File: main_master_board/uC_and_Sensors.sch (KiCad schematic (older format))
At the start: 39 parts, among them U1 NRF24L01+, U15 DSPIC33EP512GP806-I/PT, U16 DWM1000, U29 RGB_LED, U30 RGB_LED, U31 Si1900DL, U32 Si1900DL, U9 Si1900DL

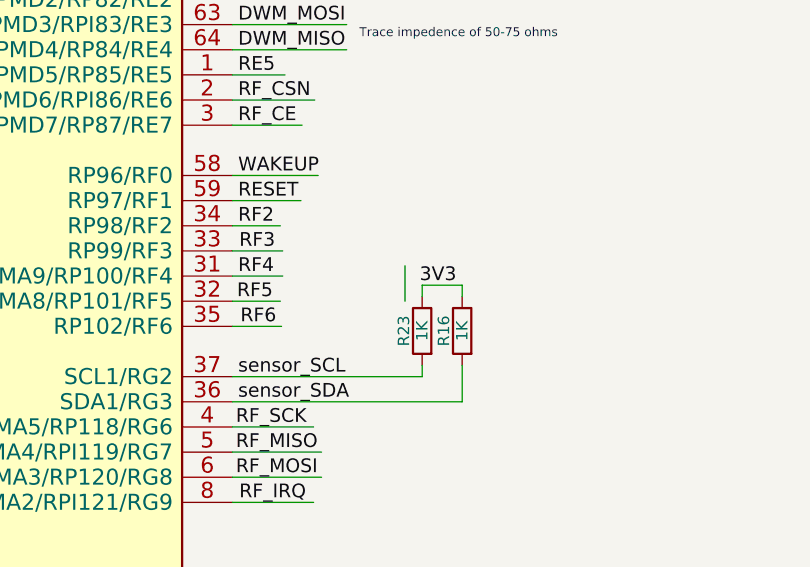
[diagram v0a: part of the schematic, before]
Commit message: Routed the 24-5 buck and added the dart board footprint
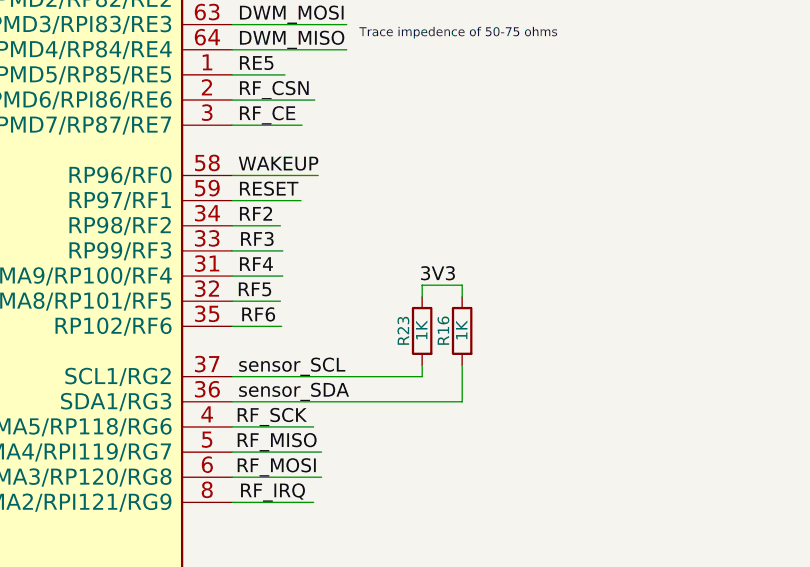
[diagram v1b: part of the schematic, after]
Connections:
- wire segments 224 -> 223
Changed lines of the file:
@@
 LIBS:Sensors
 LIBS:LP3852-3.3
-LIBS:decaWave
+LIBS:0s102011ma1qn1
+LIBS:74LVC1G17
+LIBS:74V1T126
+LIBS:acs711klctr-12ab-t
+LIBS:AD7192
+LIBS:AD7193
+LIBS:am-hrr30-xxx
+LIBS:aon7528
+LIBS:AP7363
+LIBS:AS1359
+LIBS:csd16323q3
+LIBS:dmn2004dmk
+LIBS:dp_devices
+LIBS:DSPIC33E128MC506
+LIBS:fds6898az
+LIBS:ina197
+LIBS:irf7329pbf
+LIBS:ld1117
+LIBS:lm3478
+LIBS:lm3481
+LIBS:lt1910
+LIBS:ltc1871
+LIBS:ltc1982
+LIBS:MAG3110
+LIBS:mcp1700
+LIBS:mcp73831
+LIBS:mcsmt-g5030a1-3712
+LIBS:microchip_can
+LIBS:microclasp_hdrx2
+LIBS:microclasp_hdrx3
+LIBS:MPU-6000_MPU-6050
+LIBS:MPU-9150
+LIBS:nrf24l01+
+LIBS:pds1040l
+LIBS:pic12f1571
+LIBS:pinhead
+LIBS:psmn013-80ys
+LIBS:RESISTOR_ARRAY
+LIBS:rf803d
+LIBS:RGB_LED
+LIBS:Si1970DH
+LIBS:sn65hvd232
+LIBS:ssc54
+LIBS:sw_push_4
+LIBS:tc74
+LIBS:TPS2113A
+LIBS:tps54540
+LIBS:vs-mbrb1635pbf
+LIBS:xal5050-562meb
+LIBS:xal6030-182mec
 LIBS:conn_2x50
 LIBS:conn_open_q_x2
@@
 LIBS:ac-dc
 LIBS:actel
-LIBS:allegro
 LIBS:Altera
 LIBS:analog_devices
@@
 LIBS:logo
 LIBS:maxim
-LIBS:mechanical
 LIBS:microchip_dspic33dsc
 LIBS:microchip_pic10mcu
@@
 LIBS:microchip_pic32mcu
 LIBS:motor_drivers
-LIBS:motors
 LIBS:msp430
 LIBS:nordicsemi
@@
 LIBS:ttl_ieee
 LIBS:video
-LIBS:wiznet
 LIBS:Worldsemi
 LIBS:Xicor
-LIBS:zetex
 LIBS:Zilog
 LIBS:conn_2x45
@@
 Text HLabel 1350 2400 0    60   Input ~ 0
 prog_UART_TX
-Wire Wire Line
-	13625 5895 13625 5740
 Text HLabel 15400 1625 2    60   Output ~ 0
 sensor_SDA

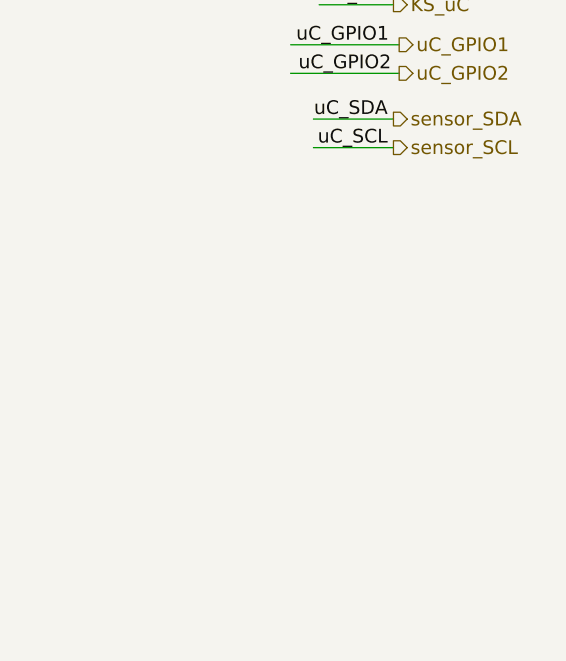
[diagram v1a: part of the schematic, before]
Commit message: Routing power. Added 5V leveling cap.
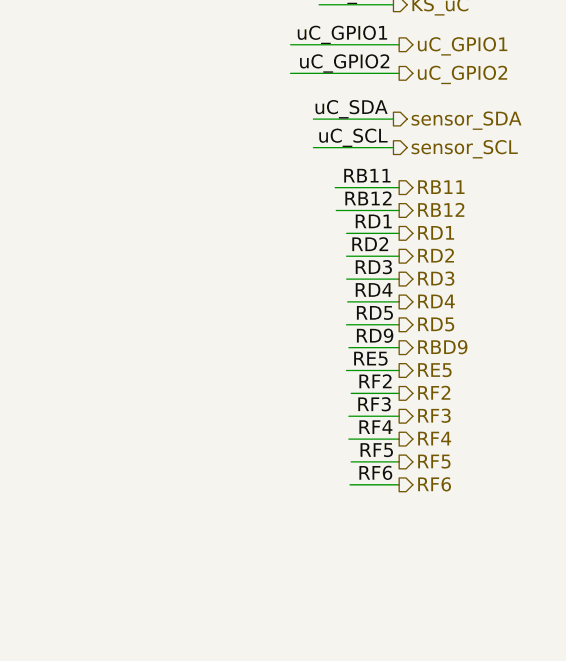
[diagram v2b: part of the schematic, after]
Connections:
- net labels added: RBD9
- wire segments 223 -> 237
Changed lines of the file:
@@
 $Descr A3 16535 11693
 encoding utf-8
-Sheet 4 6
+Sheet 4 5
 Title ""
 Date ""
@@
 Wire Wire Line
 	6175 3850 6450 3850
+Text Label 15400 2125 2    60   ~ 0
+RD1
+Text Label 15385 2225 2    60   ~ 0
+RD2
+Text Label 15400 2325 2    60   ~ 0
+RD3
+Text Label 15400 2425 2    60   ~ 0
+RD4
+Text Label 15405 2525 2    60   ~ 0
+RD5
+Wire Wire Line
+	15425 2525 15195 2525
+Wire Wire Line
+	15425 2425 15200 2425
+Wire Wire Line
+	15425 2325 15195 2325
+Wire Wire Line
+	15425 2225 15195 2225
+Wire Wire Line
+	15425 2125 15195 2125
+Text Label 15395 1925 2    60   ~ 0
+RB11
+Text Label 15400 2025 2    60   ~ 0
+RB12
+Wire Wire Line
+	15150 2025 15425 2025
+Wire Wire Line
+	15425 1925 15145 1925
+Text Label 15405 2625 2    60   ~ 0
+RD9
+Wire Wire Line
+	15425 2625 15205 2625
+Text Label 15400 3225 2    60   ~ 0
+RF6
+Text Label 15395 2925 2    60   ~ 0
+RF3
+Text Label 15400 2825 2    60   ~ 0
+RF2
+Text Label 15400 3025 2    60   ~ 0
+RF4
+Text Label 15405 3125 2    60   ~ 0
+RF5
+Wire Wire Line
+	15425 2825 15215 2825
+Wire Wire Line
+	15425 2925 15205 2925
+Wire Wire Line
+	15425 3025 15205 3025
+Wire Wire Line
+	15425 3125 15215 3125
+Wire Wire Line
+	15425 3225 15210 3225
+Text Label 15220 2725 0    60   ~ 0
+RE5
+Wire Wire Line
+	15195 2725 15425 2725
+Text HLabel 15425 2125 2    60   Output ~ 0
+RD1
+Text HLabel 15425 2225 2    60   Output ~ 0
+RD2
+Text HLabel 15425 2325 2    60   Output ~ 0
+RD3
+Text HLabel 15425 2425 2    60   Output ~ 0
+RD4
+Text HLabel 15425 2525 2    60   Output ~ 0
+RD5
+Text HLabel 15425 1925 2    60   Output ~ 0
+RB11
+Text HLabel 15425 2025 2    60   Output ~ 0
+RB12
+Text HLabel 15425 2625 2    60   Output ~ 0
+RBD9
+Text HLabel 15425 2825 2    60   Output ~ 0
+RF2
+Text HLabel 15425 2925 2    60   Output ~ 0
+RF3
+Text HLabel 15425 3025 2    60   Output ~ 0
+RF4
+Text HLabel 15425 3125 2    60   Output ~ 0
+RF5
+Text HLabel 15425 3225 2    60   Output ~ 0
+RF6
+Text HLabel 15425 2725 2    60   Output ~ 0
+RE5
 $EndSCHEMATC

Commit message: Working on routing near n-p mosfets. save point incase new apporach doesn't work out
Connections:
- net labels added: shutdown_int, uC_kill
- net labels removed: RBD9, RD9, RF2
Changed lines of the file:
@@
 LIBS:Sensors
 LIBS:LP3852-3.3
-LIBS:0s102011ma1qn1
-LIBS:74LVC1G17
-LIBS:74V1T126
-LIBS:acs711klctr-12ab-t
-LIBS:AD7192
-LIBS:AD7193
-LIBS:am-hrr30-xxx
-LIBS:aon7528
-LIBS:AP7363
-LIBS:AS1359
-LIBS:csd16323q3
-LIBS:dmn2004dmk
-LIBS:dp_devices
-LIBS:DSPIC33E128MC506
-LIBS:fds6898az
-LIBS:ina197
-LIBS:irf7329pbf
-LIBS:ld1117
-LIBS:lm3478
-LIBS:lm3481
-LIBS:lt1910
-LIBS:ltc1871
-LIBS:ltc1982
-LIBS:MAG3110
-LIBS:mcp1700
-LIBS:mcp73831
-LIBS:mcsmt-g5030a1-3712
-LIBS:microchip_can
-LIBS:microclasp_hdrx2
-LIBS:microclasp_hdrx3
-LIBS:MPU-6000_MPU-6050
-LIBS:MPU-9150
-LIBS:nrf24l01+
-LIBS:pds1040l
-LIBS:pic12f1571
-LIBS:pinhead
-LIBS:psmn013-80ys
-LIBS:RESISTOR_ARRAY
-LIBS:rf803d
-LIBS:RGB_LED
-LIBS:Si1970DH
-LIBS:sn65hvd232
-LIBS:ssc54
-LIBS:sw_push_4
-LIBS:tc74
-LIBS:TPS2113A
-LIBS:tps54540
-LIBS:vs-mbrb1635pbf
-LIBS:xal5050-562meb
-LIBS:xal6030-182mec
+LIBS:decaWave
 LIBS:conn_2x50
 LIBS:conn_open_q_x2
@@
 LIBS:ac-dc
 LIBS:actel
+LIBS:allegro
 LIBS:Altera
 LIBS:analog_devices
@@
 LIBS:logo
 LIBS:maxim
+LIBS:mechanical
 LIBS:microchip_dspic33dsc
 LIBS:microchip_pic10mcu
@@
 LIBS:microchip_pic32mcu
 LIBS:motor_drivers
+LIBS:motors
 LIBS:msp430
 LIBS:nordicsemi
@@
 LIBS:ttl_ieee
 LIBS:video
+LIBS:wiznet
 LIBS:Worldsemi
 LIBS:Xicor
+LIBS:zetex
 LIBS:Zilog
 LIBS:conn_2x45
@@
 Text Label 9110 6115 2    60   ~ 0
 RD5
-Text Label 9110 6555 2    60   ~ 0
-RD9
 Text Label 12905 6005 0    60   ~ 0
 RF6
 Text Label 12900 5675 0    60   ~ 0
 RF3
-Text Label 12895 5565 0    60   ~ 0
-RF2
 Text Label 12895 4905 0    60   ~ 0
 RE5
@@
 RF5
 Wire Wire Line
-	12870 5565 13080 5565
+	12870 5565 13200 5565
 Wire Wire Line
 	12870 5675 13090 5675
@@
 uC_UART_TX
 Wire Wire Line
-	9130 6555 8910 6555
+	8525 6555 9130 6555
 Wire Wire Line
 	9130 6115 8900 6115
@@
 Wire Wire Line
 	15425 1925 15145 1925
-Text Label 15405 2625 2    60   ~ 0
-RD9
-Wire Wire Line
-	15425 2625 15205 2625
-Text Label 15400 3225 2    60   ~ 0
+Text Label 15400 3025 2    60   ~ 0
 RF6
-Text Label 15395 2925 2    60   ~ 0
+Text Label 15395 2725 2    60   ~ 0
 RF3
 Text Label 15400 2825 2    60   ~ 0
-RF2
-Text Label 15400 3025 2    60   ~ 0
 RF4
-Text Label 15405 3125 2    60   ~ 0
+Text Label 15405 2925 2    60   ~ 0
 RF5
 Wire Wire Line
-	15425 2825 15215 2825
-Wire Wire Line
-	15425 2925 15205 2925
-Wire Wire Line
-	15425 3025 15205 3025
-Wire Wire Line
-	15425 3125 15215 3125
-Wire Wire Line
-	15425 3225 15210 3225
-Text Label 15220 2725 0    60   ~ 0
+	15425 2725 15205 2725
+Wire Wire Line
+	15425 2825 15205 2825
+Wire Wire Line
+	15425 2925 15215 2925
+Wire Wire Line
+	15425 3025 15210 3025
+Text Label 15220 2625 0    60   ~ 0
 RE5
 Wire Wire Line
-	15195 2725 15425 2725
+	15195 2625 15425 2625
 Text HLabel 15425 2125 2    60   Output ~ 0
 RD1
@@
 Text HLabel 15425 2025 2    60   Output ~ 0
 RB12
+Text HLabel 15425 2725 2    60   Output ~ 0
+RF3
+Text HLabel 15425 2825 2    60   Output ~ 0
+RF4
+Text HLabel 15425 2925 2    60   Output ~ 0
+RF5
+Text HLabel 15425 3025 2    60   Output ~ 0
+RF6
 Text HLabel 15425 2625 2    60   Output ~ 0
-RBD9
-Text HLabel 15425 2825 2    60   Output ~ 0
-RF2
-Text HLabel 15425 2925 2    60   Output ~ 0
-RF3
-Text HLabel 15425 3025 2    60   Output ~ 0
-RF4
-Text HLabel 15425 3125 2    60   Output ~ 0
-RF5
-Text HLabel 15425 3225 2    60   Output ~ 0
-RF6
-Text HLabel 15425 2725 2    60   Output ~ 0
 RE5
+Text HLabel 1325 3200 0    60   Input ~ 0
+shutdown_int
+Text Label 1350 3200 0    60   ~ 0
+shutdown_int
+Wire Wire Line
+	1325 3200 1950 3200
+Text Label 9110 6555 2    60   ~ 0
+shutdown_int
+Text Label 12895 5565 0    60   ~ 0
+uC_kill
+Text HLabel 15425 3200 2    60   Output ~ 0
+uC_kill
+Text Label 15400 3200 2    60   ~ 0
+uC_kill
+Wire Wire Line
+	15425 3200 15075 3200
 $EndSCHEMATC

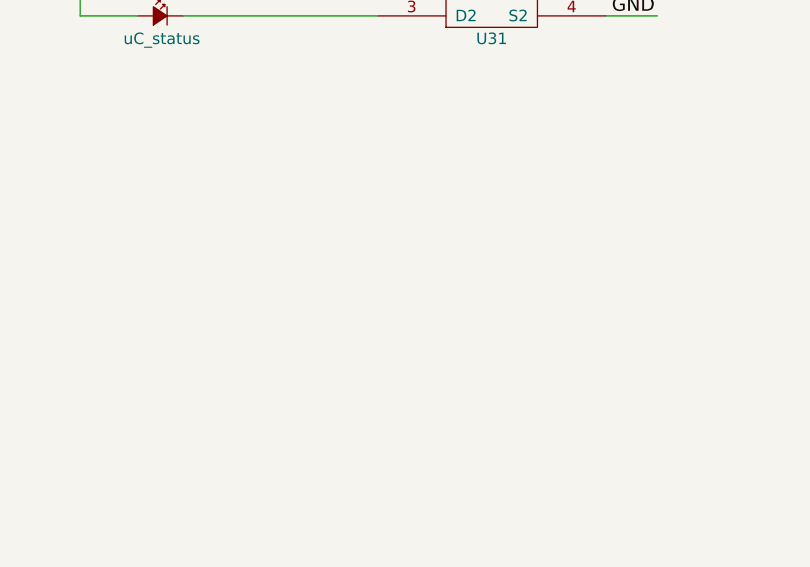
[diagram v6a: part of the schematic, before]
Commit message: Changed expansion connector to two connectors. Routed 5 to 4 buck.
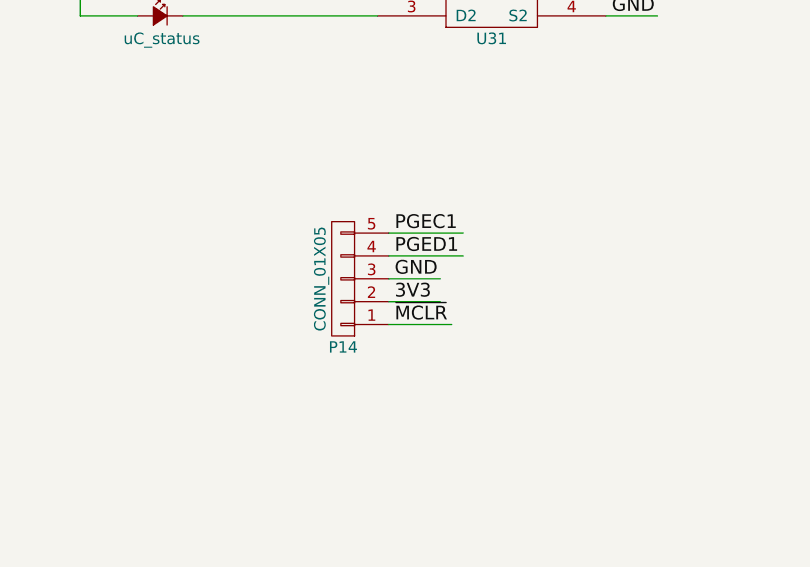
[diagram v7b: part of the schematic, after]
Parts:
- added P14: CONN_01X05, Pin_Headers:Pin_Header_Angled_1x05_Pitch1.27mm, symbol CONN_01X05
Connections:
- wire segments 237 -> 242
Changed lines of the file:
@@
 Wire Wire Line
 	15425 3200 15075 3200
+$Comp
+L CONN_01X05 P14
+U 1 1 589408D8
+P 5000 5875
+F 0 "P14" H 5000 6175 50  0000 C CNN
+F 1 "CONN_01X05" V 5100 5875 50  0000 C CNN
+F 2 "Pin_Headers:Pin_Header_Angled_1x05_Pitch1.27mm" H 5000 5875 50  0001 C CNN
+F 3 "" H 5000 5875 50  0000 C CNN
+	1    5000 5875
+	-1   0    0    1
+$EndComp
+Text Label 5225 6075 0    60   ~ 0
+~MCLR
+Text Label 5225 5975 0    60   ~ 0
+3V3
+Text Label 5225 5875 0    60   ~ 0
+GND
+Text Label 5225 5775 0    60   ~ 0
+PGED1
+Text Label 5225 5675 0    60   ~ 0
+PGEC1
+Wire Wire Line
+	5200 5675 5525 5675
+Wire Wire Line
+	5200 5775 5525 5775
+Wire Wire Line
+	5200 5875 5425 5875
+Wire Wire Line
+	5200 5975 5425 5975
+Wire Wire Line
+	5200 6075 5475 6075
 $EndSCHEMATC
